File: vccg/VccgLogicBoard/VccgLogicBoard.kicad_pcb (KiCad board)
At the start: 2 copper layers, 50.8 x 103.4 mm, 72 parts, among them J1 ChordCV, J10 root, J11 chord1, J2 OctaveCV, J3 MelodyCV, J4 MelodyClock, J5 ChordClock, J6 Conn_02x05_Odd_Even, J7 oled, J8 melody, J9 chord2, M1 RaspberryPiPico, Q1 MMBT3904, Q2 MMBT3904, SW1 Back, SW2 RotaryEncoder_Switch, U1 MCP6002-xSN, U2 MCP6002-xSN, U3 74HC14, U4 XL1509, U5 MCP4728, U6 LM2904, U7 LM2904

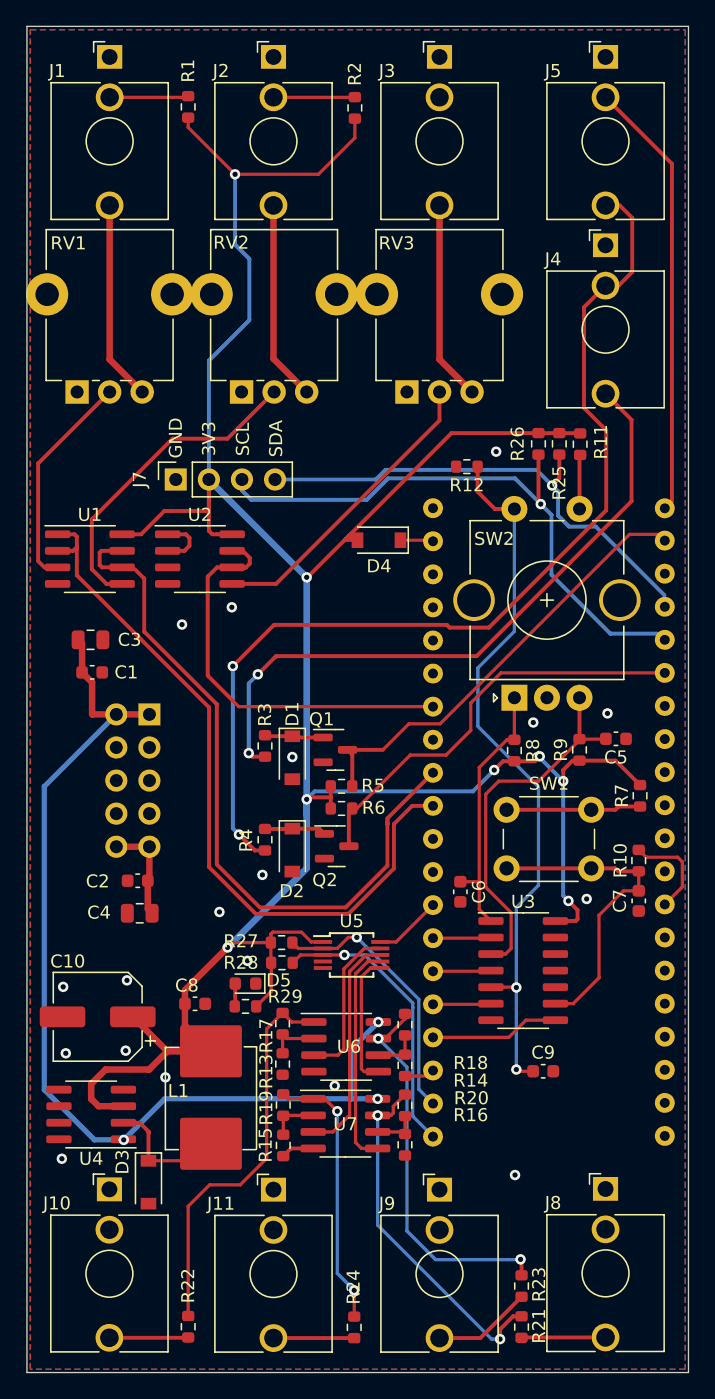
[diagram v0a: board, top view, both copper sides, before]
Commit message: Rebuild with 4 mom buttons instead of rotary encoder
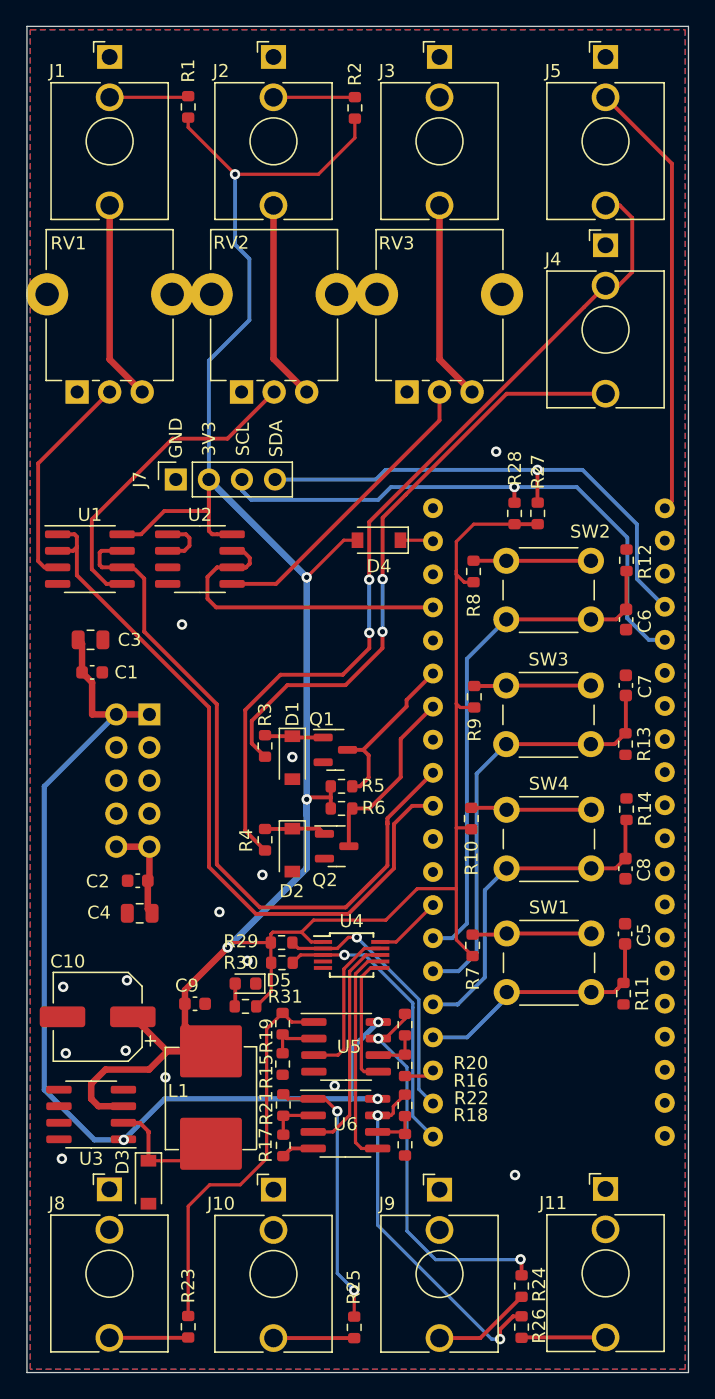
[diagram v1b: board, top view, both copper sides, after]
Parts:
- removed the C9 at (234.5, 108.2)
- removed the R25 at (235.7, 60.0)
- removed the R26 at (234.1, 60.0)
- removed the U3 at (232.9, 100.5)
- added C7: 10n, Capacitor_SMD:C_0603_1608Metric, F.Cu at (240.8, 78.5)
- added R13: 100K, Resistor_SMD:R_0603_1608Metric, F.Cu at (240.8, 83.1)
- added R27: 100K, Resistor_SMD:R_0603_1608Metric, F.Cu at (234.0, 65.3)
- added R28: 100K, Resistor_SMD:R_0603_1608Metric, F.Cu at (232.3, 65.3)
- added R7: 1K, Resistor_SMD:R_0603_1608Metric, F.Cu at (229.0, 98.5)
- added SW1: Down, Button_Switch_THT:SW_PUSH_6mm_H13mm, F.Cu at (231.7, 97.6)
- added SW3: Select, Button_Switch_THT:SW_PUSH_6mm_H13mm, F.Cu at (231.6, 78.6)
- R11: value 1K -> 100K
- R8, R9: value 10K -> 1K
- SW2: value RotaryEncoder_Switch -> Up; footprint Rotary_Encoder:RotaryEncoder_Alps_EC11E-Switch_Vertical_H20mm_CircularMountingHoles -> Button_Switch_THT:SW_PUSH_6mm_H13mm
- moved R11 42.3 mm to (240.6, 102.2)
- moved C6 24.5 mm to (240.8, 73.5)
- moved C5 15.0 mm to (240.8, 97.6), turned to 90 degrees
- moved R12 14.2 mm to (240.9, 68.9), turned to 90 degrees
- moved R8 14.1 mm to (229.1, 69.8), turned to 90 degrees
- moved R10 13.1 mm to (228.9, 88.8), turned to 90 degrees
- moved SW2 10.5 mm to (231.6, 69.0), turned to 0 degrees
- moved R9 9.05 mm to (229.2, 79.4)
- moved R14 4.06 mm to (240.9, 88.1)
- moved C8 2.68 mm to (240.8, 92.6)
- renumbered C7 to C8, C8 to C9, J11 to J10, J8 to J11, J10 to J8, R7 to R10, R10 to R14, R13 to R15, R14 to R16, R15 to R17, R16 to R18, R17 to R19, R18 to R20, R19 to R21, R20 to R22, R22 to R23, R23 to R24, R24 to R25, R21 to R26, R27 to R29, R28 to R30, R29 to R31, SW1 to SW4, U4 to U3, U5 to U4, U6 to U5, U7 to U6
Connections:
- C5 pad 1: GND -> down
- C5 pad 2: encoderB -> GND
- C6 pad 1: encoderA -> up
- M1 pad 2: melodyClock -> unconnected-(M1-Pad2)
- M1 pad 24: debounceBack -> down
- M1 pad 25: debounceSelect -> back
- M1 pad 26: debounceB -> select
- M1 pad 27: debounceA -> up
- M1 pad 34: melody -> chordClock
- M1 pad 35: unconnected-(M1-Pad35) -> melodyClock
- M1 pad 37: unconnected-(M1-Pad37) -> melody
- M1 pad 6: chordClock -> unconnected-(M1-Pad6)
- R11 pad 1: +3V3 -> down
- R11 pad 2: Net-(R11-Pad2) -> GND
- R12 pad 1: select -> up
- R8 pad 1: encoderA -> +3V3
- R8 pad 2: +3V3 -> Net-(R8-Pad2)
- R9 pad 2: encoderB -> Net-(R9-Pad2)
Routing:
- net up: track 0.00 -> 40.2 mm
- net encoderB: track 28.6 -> 0.00 mm
- net select: track 55.4 -> 33.3 mm, vias 2 -> 0
- net melodyClock: track 34.4 -> 13.1 mm
- net encoderA: track 20.4 -> 0.00 mm
- net down: track 0.00 -> 19.7 mm
- net chordClock: track 32.6 -> 14.2 mm
- net debounceBack: track 9.95 -> 0.00 mm
- net Net-(J4-PadTN): track 77.2 -> 67.4 mm
- net Net-(R7-Pad2): track 0.00 -> 9.16 mm
- net Net-(R8-Pad2): track 0.00 -> 9.02 mm
- net Net-(R9-Pad2): track 0.00 -> 8.96 mm
- net +3V3: track 217.4 -> 208.8 mm, vias 8 -> 4
- net GND: track 17.7 -> 10.1 mm, vias 18 -> 14
- net melody: track 31.6 -> 25.0 mm
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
